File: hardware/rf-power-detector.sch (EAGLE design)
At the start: 36 parts, among them U1 AD8317, U4 MIC5301

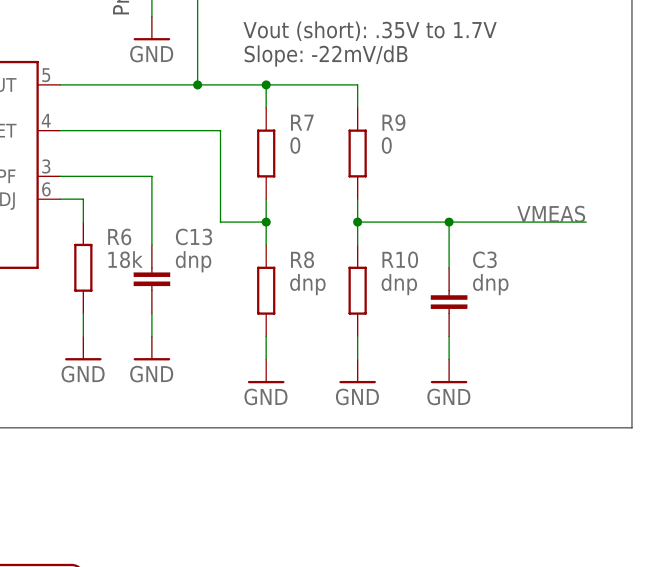
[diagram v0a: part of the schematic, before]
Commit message: hw: add a 150Ohm load on the adc input
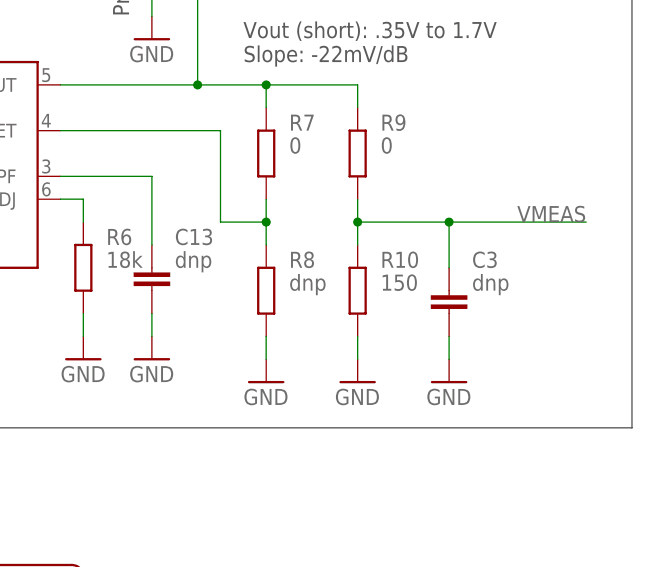
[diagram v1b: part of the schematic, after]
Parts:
- R10: value dnp -> 150
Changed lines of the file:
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@@
 <part name="GND24" library="supply1" deviceset="GND" device=""/>
 <part name="R9" library="rcl" deviceset="R-EU_" device="R0603" value="0"/>
-<part name="R10" library="rcl" deviceset="R-EU_" device="R0603" value="dnp"/>
+<part name="R10" library="rcl" deviceset="R-EU_" device="R0603" value="150"/>
 <part name="GND25" library="supply1" deviceset="GND" device=""/>
 <part name="BOX1" library="hammond" deviceset="HAMMOND-BOX" device="-1551G" value="HAMMOND-BOX-1551G"/>
